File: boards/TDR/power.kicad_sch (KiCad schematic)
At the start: 66 parts, among them U1 LFE5UM5G-45-CABGA381, U5 MIC5504-3.3YM5, U6 AP3402, U7 AP3402, U8 LD39050PUR, U9 LD39050PUR

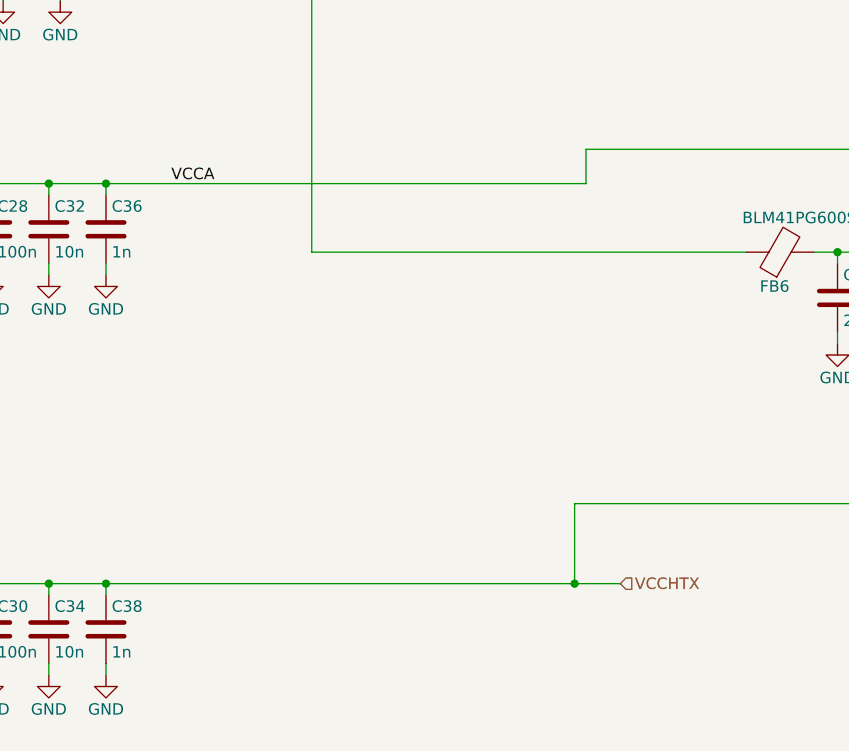
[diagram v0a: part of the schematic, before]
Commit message: change crystal footprint and roughly finish schematic
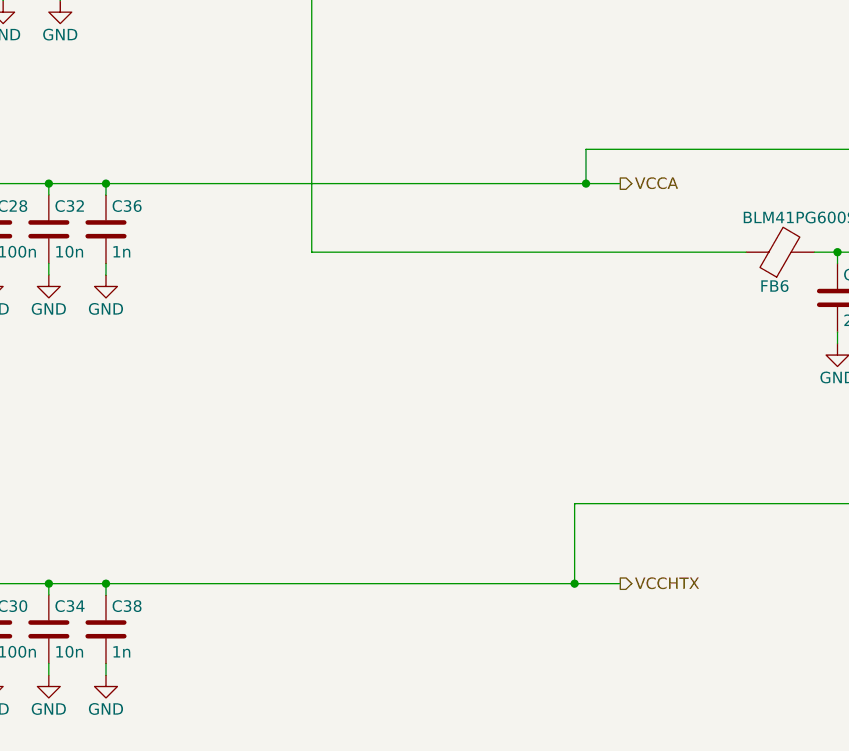
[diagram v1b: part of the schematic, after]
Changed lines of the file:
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@@
-(kicad_sch (version 20200618) (host eeschema "(5.99.0-2053-g67bd49b4a)")
+(kicad_sch (version 20200618) (host eeschema "(5.99.0-2073-gbb1afb747)")
   (page 3 5)
   (paper "A4")
   (title_block
     (title "TDR, FPGA Power")
-    (date "2020-04-17")
+    (date "2020-06-30")
     (rev "A")
     (company "Radovan Blažek")
@@
   (junction (at 189.23 53.34) (diameter 0) (color 0 0 0 0))
   (junction (at 189.23 134.62) (diameter 0) (color 0 0 0 0))
+  (junction (at 190.5 90.17) (diameter 0) (color 0 0 0 0))
   (junction (at 195.58 53.34) (diameter 0) (color 0 0 0 0))
   (junction (at 201.93 53.34) (diameter 0) (color 0 0 0 0))
@@
     (stroke (width 0) (type solid) (color 0 0 0 0))
   )
+  (wire (pts (xy 190.5 90.17) (xy 194.31 90.17))
+    (stroke (width 0) (type solid) (color 0 0 0 0))
+  )
   (wire (pts (xy 195.58 53.34) (xy 195.58 54.61))
     (stroke (width 0) (type solid) (color 0 0 0 0))
@@
     (effects (font (size 1.27 1.27)) (justify right bottom))
   )
-  (label "VCCA" (at 149.225 90.17 180)
-    (effects (font (size 1.27 1.27)) (justify right bottom))
-  )
   (label "VCCAUX" (at 254 97.79 180)
     (effects (font (size 1.27 1.27)) (justify right bottom))
@@
     (effects (font (size 1.27 1.27)) (justify left))
   )
-  (hierarchical_label "VCCHTX" (shape input) (at 194.31 134.62 0)
+  (hierarchical_label "VCCA" (shape output) (at 194.31 90.17 0)
     (effects (font (size 1.27 1.27)) (justify left))
   )
+  (hierarchical_label "VCCHTX" (shape output) (at 194.31 134.62 0)
+    (effects (font (size 1.27 1.27)) (justify left))
+  )

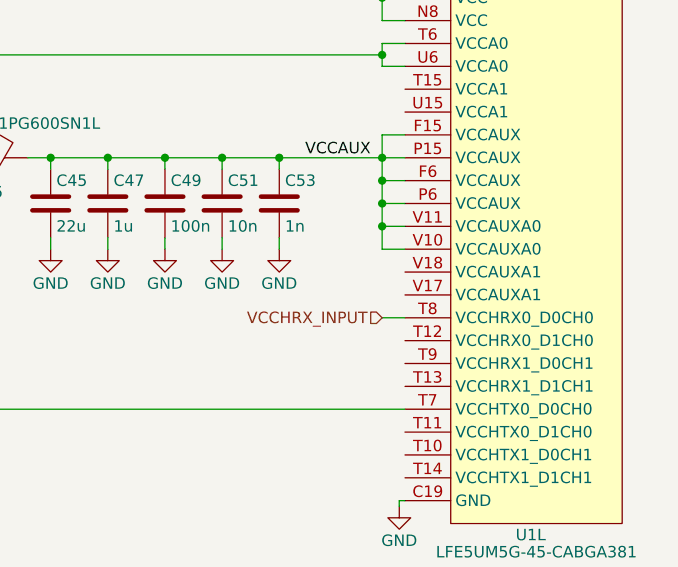
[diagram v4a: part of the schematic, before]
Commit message: solved DRC errors and routed few more nets
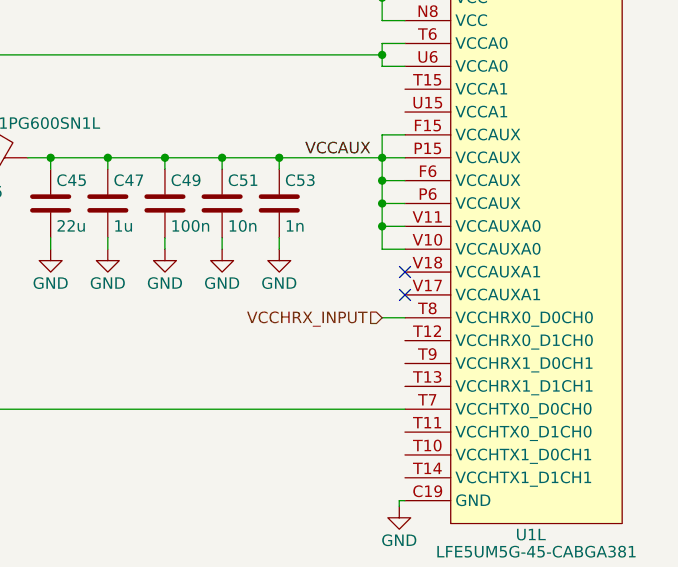
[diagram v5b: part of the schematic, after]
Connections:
- no-connect marks 0 -> 2
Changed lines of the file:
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@@
-(kicad_sch (version 20200618) (host eeschema "(5.99.0-2241-g37ce9fb84)")
+(kicad_sch (version 20200618) (host eeschema "(5.99.0-2250-gafd432e68)")
   (page 3 5)
   (paper "A4")
@@
   (junction (at 255.27 102.87) (diameter 0) (color 0 0 0 0))
   (junction (at 255.27 105.41) (diameter 0) (color 0 0 0 0))
+  (no_connect (at 257.81 110.49))
+  (no_connect (at 257.81 113.03))
   (wire (pts (xy 25.4 41.91) (xy 25.4 172.72))
     (stroke (width 0) (type solid) (color 0 0 0 0))

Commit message: finish routing
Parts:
- removed C36: 1n, Capacitor_SMD:C_0402_1005Metric, symbol Device:C
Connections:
- net VCCA: now also U1.T10 (VCCHTX1_D0CH1)
- no-connect marks 2 -> 7
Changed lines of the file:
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@@
   (junction (at 132.08 58.42) (diameter 0) (color 0 0 0 0))
   (junction (at 134.62 24.13) (diameter 0) (color 0 0 0 0))
-  (junction (at 137.16 90.17) (diameter 0) (color 0 0 0 0))
   (junction (at 137.16 134.62) (diameter 0) (color 0 0 0 0))
   (junction (at 160.02 58.42) (diameter 0) (color 0 0 0 0))
@@
   (junction (at 195.58 53.34) (diameter 0) (color 0 0 0 0))
   (junction (at 201.93 53.34) (diameter 0) (color 0 0 0 0))
+  (junction (at 203.835 86.36) (diameter 0) (color 0 0 0 0))
   (junction (at 208.28 53.34) (diameter 0) (color 0 0 0 0))
   (junction (at 214.63 53.34) (diameter 0) (color 0 0 0 0))
@@
   (no_connect (at 257.81 110.49))
   (no_connect (at 257.81 113.03))
+  (no_connect (at 257.81 118.11))
+  (no_connect (at 257.81 123.19))
+  (no_connect (at 257.81 128.27))
+  (no_connect (at 257.81 133.35))
+  (no_connect (at 257.81 120.65))
   (wire (pts (xy 25.4 41.91) (xy 25.4 172.72))
     (stroke (width 0) (type solid) (color 0 0 0 0))
@@
     (stroke (width 0) (type solid) (color 0 0 0 0))
   )
-  (wire (pts (xy 130.81 90.17) (xy 137.16 90.17))
+  (wire (pts (xy 130.81 90.17) (xy 190.5 90.17))
     (stroke (width 0) (type solid) (color 0 0 0 0))
   )
@@
     (stroke (width 0) (type solid) (color 0 0 0 0))
   )
-  (wire (pts (xy 137.16 90.17) (xy 137.16 91.44))
-    (stroke (width 0) (type solid) (color 0 0 0 0))
-  )
-  (wire (pts (xy 137.16 90.17) (xy 190.5 90.17))
-    (stroke (width 0) (type solid) (color 0 0 0 0))
-  )
-  (wire (pts (xy 137.16 99.06) (xy 137.16 100.33))
-    (stroke (width 0) (type solid) (color 0 0 0 0))
-  )
   (wire (pts (xy 137.16 134.62) (xy 137.16 135.89))
     (stroke (width 0) (type solid) (color 0 0 0 0))
@@
     (stroke (width 0) (type solid) (color 0 0 0 0))
   )
-  (wire (pts (xy 190.5 86.36) (xy 255.27 86.36))
+  (wire (pts (xy 190.5 86.36) (xy 203.835 86.36))
     (stroke (width 0) (type solid) (color 0 0 0 0))
   )
@@
   )
   (wire (pts (xy 201.93 62.23) (xy 201.93 63.5))
+    (stroke (width 0) (type solid) (color 0 0 0 0))
+  )
+  (wire (pts (xy 203.835 86.36) (xy 203.835 130.81))
+    (stroke (width 0) (type solid) (color 0 0 0 0))
+  )
+  (wire (pts (xy 203.835 86.36) (xy 255.27 86.36))
+    (stroke (width 0) (type solid) (color 0 0 0 0))
+  )
+  (wire (pts (xy 203.835 130.81) (xy 257.81 130.81))
     (stroke (width 0) (type solid) (color 0 0 0 0))
   )
@@
     )
   )
-  (symbol (lib_id "power:GND") (at 137.16 100.33 0) (unit 1)
-    (in_bom yes) (on_board yes)
-    (property "Reference" "#PWR0160" (id 0) (at 137.16 106.68 0)
-      (effects (font (size 1.27 1.27)) hide)
-    )
-    (property "Value" "GND" (id 1) (at 137.16 104.14 0))
-    (property "Footprint" "" (id 2) (at 137.16 100.33 0)
-      (effects (font (size 1.27 1.27)) hide)
-    )
-    (property "Datasheet" "" (id 3) (at 137.16 100.33 0)
-      (effects (font (size 1.27 1.27)) hide)
-    )
-  )
   (symbol (lib_id "power:GND") (at 137.16 144.78 0) (unit 1)
     (in_bom yes) (on_board yes)
@@
       (effects (font (size 1.27 1.27)) hide)
     )
-  )
-  (symbol (lib_id "Device:C") (at 137.16 95.25 0) (unit 1)
-    (in_bom yes) (on_board yes)
-    (property "Reference" "C36" (id 0) (at 137.795 92.71 0)
-      (effects (font (size 1.27 1.27)) (justify left))
-    )
-    (property "Value" "1n" (id 1) (at 137.795 97.79 0)
-      (effects (font (size 1.27 1.27)) (justify left))
-    )
-    (property "Footprint" "Capacitor_SMD:C_0402_1005Metric" (id 2) (at 138.1252 99.06 0)
-      (effects (font (size 1.27 1.27)) hide)
-    )
-    (property "Datasheet" "~" (id 3) (at 137.16 95.25 0)
-      (effects (font (size 1.27 1.27)) hide)
-    )

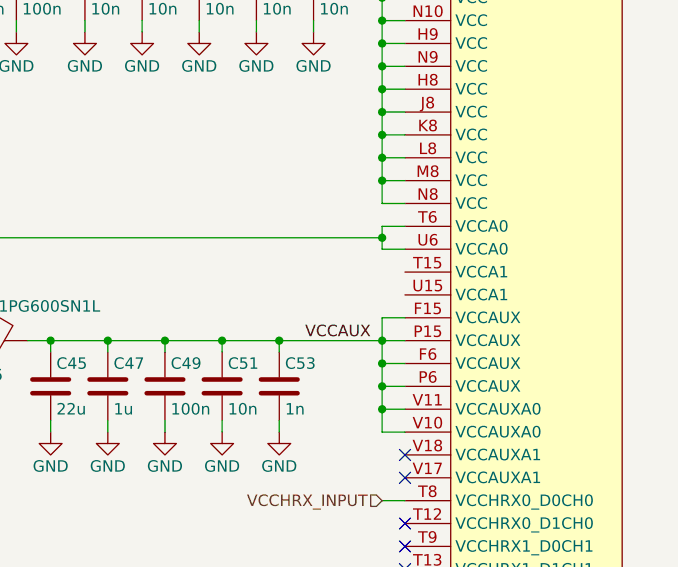
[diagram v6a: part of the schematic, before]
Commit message: finishing touches on the silkscreen
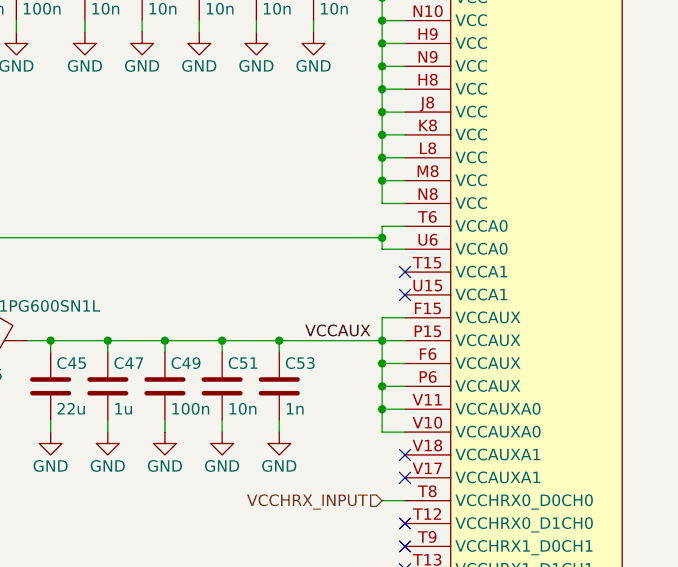
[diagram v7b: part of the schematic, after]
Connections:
- no-connect marks 7 -> 9
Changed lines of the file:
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@@
   (junction (at 255.27 102.87) (diameter 0) (color 0 0 0 0))
   (junction (at 255.27 105.41) (diameter 0) (color 0 0 0 0))
+  (no_connect (at 257.81 90.17))
+  (no_connect (at 257.81 92.71))
   (no_connect (at 257.81 110.49))
   (no_connect (at 257.81 113.03))

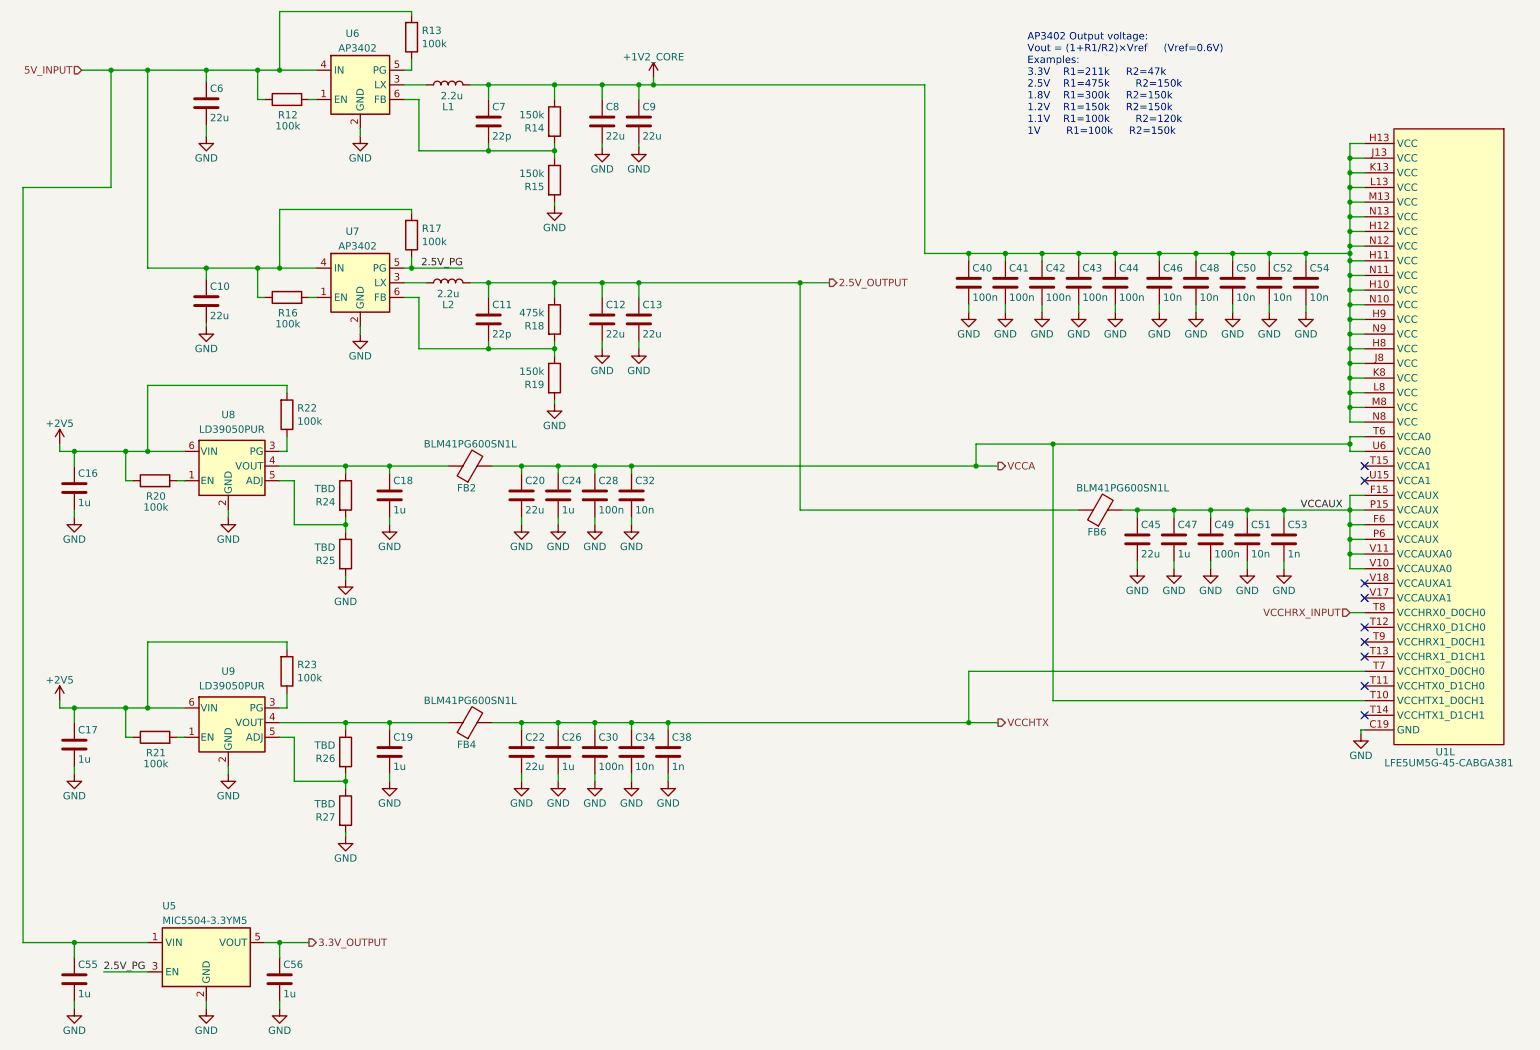
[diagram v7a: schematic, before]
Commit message: Add LD39050PUR feedback resistor values, fixed regulator enable
Fixes #1
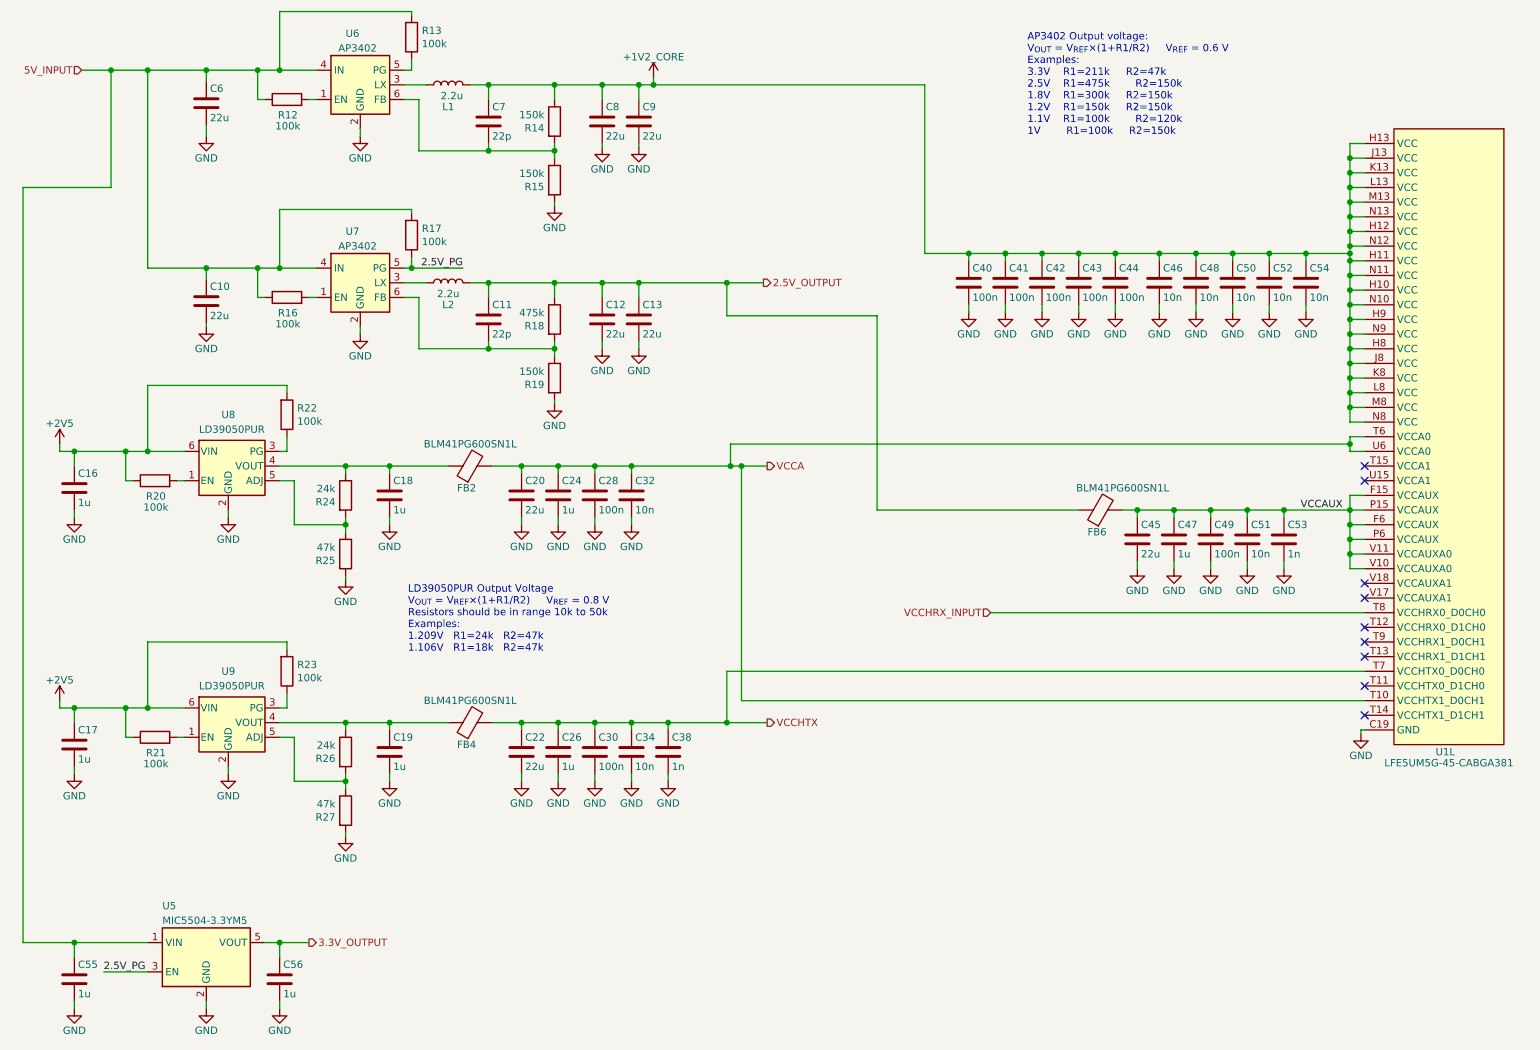
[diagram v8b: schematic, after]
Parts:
- R24, R26: value TBD -> 24k
- R25, R27: value TBD -> 47k
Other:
- note added: "AP3402 Output voltage: V_{OUT} = V_{REF}×(1+R1/R2) V_{REF} = 0.6 V Examples: 3.3V R1=211k R2=47k 2.5V R1=475k R2=150k 1.8V R1=300k R2=150k 1.2V R1=150k R2=150k 1.1V R1=100k R2=120k 1V R1=100k R2=150k"
- note added: "LD39050PUR Output Voltage V_{OUT} = V_{REF}×(1+R1/R2) V_{REF} = 0.8 V Resistors should be in range 10k to 50k Examples: 1.209V R1=24k R2=47k 1.106V R1=18k R2=47k"
- note removed: "AP3402 Output voltage: Vout = (1+R1/R2)×Vref (Vref=0.6V) Examples: 3.3V R1=211k R2=47k 2.5V R1=475k R2=150k 1.8V R1=300k R2=150k 1.2V R1=150k R2=150k 1.1V R1=100k R2=120k 1V R1=100k R2=150k"
